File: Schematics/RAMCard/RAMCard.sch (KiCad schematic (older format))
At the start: 8 parts, among them U1 74LS32, U2 74LS04, U3 IDT71256SA12TPG, U4 IDT71256SA12TPG

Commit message: Update RAMCard to include PI and PO signals.
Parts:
- removed U1: 74LS32, Package_DIP:DIP-14_W7.62mm, symbol 74xx:74LS32
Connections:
- net labels added: ~PI, ~PO
- net labels removed: DeviceSelect5, DeviceSelect[0..7], ~MI, ~MO
- wire segments 76 -> 69
- no-connect marks 16 -> 10
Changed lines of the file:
@@
 encoding utf-8
 Sheet 1 1
-Title ""
+Title "RAM Card"
 Date ""
 Rev ""
@@
 Wire Bus Line
 	5850 1250 1900 1250
-Text GLabel 1850 2000 0    50   Input ~ 0
-DeviceSelect[0..7]
-Text GLabel 1850 1700 0    50   Input ~ 0
-~MI
-$Comp
-L 74xx:74LS32 U?
-U 2 1 5E2163C3
-P 4700 2400
-AR Path="/5D2C0C74/5E2163C3" Ref="U?"  Part="1"
-AR Path="/5D2C1188/5E2163C3" Ref="U?"  Part="2"
-AR Path="/5E2163C3" Ref="U1"  Part="2"
-F 0 "U1" H 4700 2725 50  0000 C CNN
-F 1 "74LS32" H 4700 2634 50  0000 C CNN
-F 2 "Package_DIP:DIP-14_W7.62mm" H 4700 2400 50  0001 C CNN
-F 3 "http://www.ti.com/lit/gpn/sn74LS32" H 4700 2400 50  0001 C CNN
-	2    4700 2400
-	1    0    0    -1
-$EndComp
-Text GLabel 1850 2500 0    50   Input ~ 0
-~MO
-Wire Bus Line
-	1850 2000 1900 2000
-Text Label 2050 2100 0    50   ~ 0
-DeviceSelect5
-Entry Wire Line
-	1900 2000 2000 2100
-Wire Wire Line
-	4250 2100 2000 2100
-$Comp
-L 74xx:74LS32 U?
-U 1 1 5E2163CE
-P 4700 1800
-AR Path="/5D2C0C74/5E2163CE" Ref="U?"  Part="1"
-AR Path="/5D2C1188/5E2163CE" Ref="U?"  Part="1"
-AR Path="/5E2163CE" Ref="U1"  Part="1"
-F 0 "U1" H 4700 2125 50  0000 C CNN
-F 1 "74LS32" H 4700 2034 50  0000 C CNN
-F 2 "Package_DIP:DIP-14_W7.62mm" H 4700 1800 50  0001 C CNN
-F 3 "http://www.ti.com/lit/gpn/sn74LS32" H 4700 1800 50  0001 C CNN
-	1    4700 1800
-	1    0    0    -1
-$EndComp
-Wire Wire Line
-	4400 1700 1850 1700
-Wire Wire Line
-	4400 1900 4250 1900
-Wire Wire Line
-	4250 1900 4250 2100
-Wire Wire Line
-	1850 2500 4400 2500
-Wire Wire Line
-	4250 2100 4250 2300
-Wire Wire Line
-	4250 2300 4400 2300
-Connection ~ 4250 2100
-Wire Wire Line
-	5000 1800 5700 1800
+Text GLabel 1850 1800 0    50   Input ~ 0
+~PI
+Text GLabel 1850 2400 0    50   Input ~ 0
+~PO
 Wire Wire Line
 	5700 1800 5700 2050
@@
 	5700 4350 5700 2050
 Connection ~ 5700 2050
-Wire Wire Line
-	5000 2400 5600 2400
 Wire Wire Line
 	5600 2400 5600 4450
@@
 Connection ~ 800  7750
 $Comp
-L 74xx:74LS32 U?
-U 3 1 5DB5AC2C
-P -1250 3150
-AR Path="/5D2C0C74/5DB5AC2C" Ref="U?"  Part="1"
-AR Path="/5D2C1188/5DB5AC2C" Ref="U?"  Part="3"
-AR Path="/5DB5AC2C" Ref="U1"  Part="3"
-F 0 "U1" H -1250 3475 50  0000 C CNN
-F 1 "74LS32" H -1250 3384 50  0000 C CNN
-F 2 "Package_DIP:DIP-14_W7.62mm" H -1250 3150 50  0001 C CNN
-F 3 "http://www.ti.com/lit/gpn/sn74LS32" H -1250 3150 50  0001 C CNN
-	3    -1250 3150
-	1    0    0    -1
-$EndComp
-$Comp
-L 74xx:74LS32 U?
-U 4 1 5DB5BEE6
-P -1250 3700
-AR Path="/5D2C0C74/5DB5BEE6" Ref="U?"  Part="1"
-AR Path="/5D2C1188/5DB5BEE6" Ref="U?"  Part="4"
-AR Path="/5DB5BEE6" Ref="U1"  Part="4"
-F 0 "U1" H -1250 4025 50  0000 C CNN
-F 1 "74LS32" H -1250 3934 50  0000 C CNN
-F 2 "Package_DIP:DIP-14_W7.62mm" H -1250 3700 50  0001 C CNN
-F 3 "http://www.ti.com/lit/gpn/sn74LS32" H -1250 3700 50  0001 C CNN
-	4    -1250 3700
-	1    0    0    -1
-$EndComp
-NoConn ~ -1550 3050
-NoConn ~ -1550 3250
-NoConn ~ -1550 3600
-NoConn ~ -1550 3800
-NoConn ~ -950 3700
-NoConn ~ -950 3150
-$Comp
 L 74xx:74LS04 U2
 U 4 1 5DB73163
@@
 NoConn ~ -250 4850
 NoConn ~ -250 4350
+Wire Wire Line
+	1850 2400 5600 2400
+Wire Wire Line
+	1850 1800 5700 1800
 Wire Bus Line
 	5850 1250 5850 5350

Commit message: Layout a PCB for the RAM card
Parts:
- removed C4: 100nF, Capacitor_THT:C_Disc_D4.3mm_W1.9mm_P5.00mm, symbol Device:C
- removed unit 2 of U2
- removed unit 4 of U2
- removed unit 3 of U2
- removed unit 5 of U2
- removed unit 6 of U2
- added J1: Device 2, Connector_PinHeader_2.54mm:PinHeader_2x20_P2.54mm_Horizontal, symbol Connector_Generic:Conn_02x20_Top_Bottom
- renumbered U2 to U1, U3 to U2, U4 to U3
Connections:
- net AddressBus0: now also J1.3 (Pin_3)
- net AddressBus1: now also J1.4 (Pin_4)
- net AddressBus10: now also J1.13 (Pin_13)
- net AddressBus11: now also J1.14 (Pin_14)
- net AddressBus12: now also J1.15 (Pin_15)
- net AddressBus13: now also J1.16 (Pin_16)
- net AddressBus14: now also J1.17 (Pin_17)
- net AddressBus15: now also J1.18 (Pin_18)
- net AddressBus2: now also J1.5 (Pin_5)
- net AddressBus3: now also J1.6 (Pin_6)
- net AddressBus4: now also J1.7 (Pin_7)
- net AddressBus5: now also J1.8 (Pin_8)
- net AddressBus6: now also J1.9 (Pin_9)
- net AddressBus7: now also J1.10 (Pin_10)
- net AddressBus8: now also J1.11 (Pin_11)
- net AddressBus9: now also J1.12 (Pin_12)
- net DataBus0: now also J1.21 (Pin_21)
- net DataBus1: now also J1.22 (Pin_22)
- net DataBus2: now also J1.23 (Pin_23)
- net DataBus3: now also J1.24 (Pin_24)
- net DataBus4: now also J1.25 (Pin_25)
- net DataBus5: now also J1.26 (Pin_26)
- net DataBus6: now also J1.27 (Pin_27)
- net DataBus7: now also J1.28 (Pin_28)
- net GND: now also J1.1 (Pin_1), J1.31 (Pin_31), J1.32 (Pin_32), J1.33 (Pin_33), J1.34 (Pin_34), J1.35 (Pin_35), J1.36 (Pin_36), J1.37 (Pin_37), J1.38 (Pin_38), J1.39 (Pin_39), J1.40 (Pin_40)
- net VCC: now also J1.2 (Pin_2); no longer C1.1, C2.1, C3.1
- net ~PI: now also J1.29 (Pin_29)
- net ~PO: now also J1.30 (Pin_30)
- new net: C1.1, C2.1, C3.1
- no-connect marks 10 -> 2
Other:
- moved on the sheet: U1A, U2, U3

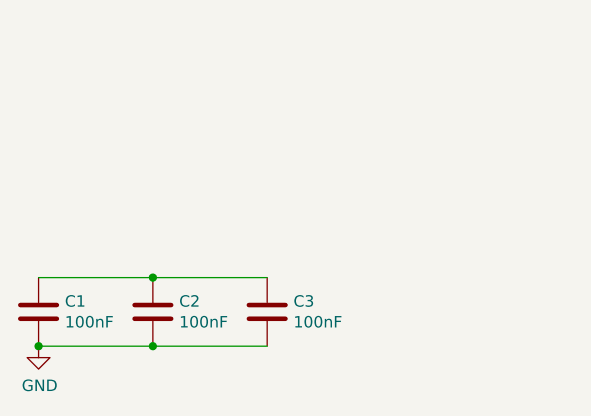
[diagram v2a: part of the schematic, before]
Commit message: Fix RAM card DRC errors
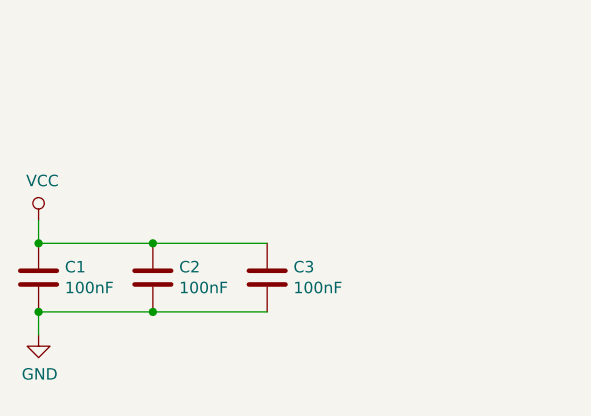
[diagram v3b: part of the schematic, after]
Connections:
- net VCC: now also C1.1, C2.1, C3.1
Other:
- moved on the sheet: C1, C2, C3
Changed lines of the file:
@@
 L Device:C C?
 U 1 1 5E262247
-P 800 7600
+P 800 7450
 AR Path="/5D2C07CD/5E262247" Ref="C?"  Part="1"
 AR Path="/5D2C1188/5E262247" Ref="C?"  Part="1"
 AR Path="/5E262247" Ref="C1"  Part="1"
-F 0 "C1" H 915 7646 50  0000 L CNN
-F 1 "100nF" H 915 7555 50  0000 L CNN
-F 2 "Capacitor_THT:C_Disc_D4.3mm_W1.9mm_P5.00mm" H 838 7450 50  0001 C CNN
-F 3 "~" H 800 7600 50  0001 C CNN
-	1    800  7600
+F 0 "C1" H 915 7496 50  0000 L CNN
+F 1 "100nF" H 915 7405 50  0000 L CNN
+F 2 "Capacitor_THT:C_Disc_D4.3mm_W1.9mm_P5.00mm" H 838 7300 50  0001 C CNN
+F 3 "~" H 800 7450 50  0001 C CNN
+	1    800  7450
 	1    0    0    -1
 $EndComp
@@
 L Device:C C?
 U 1 1 5E26224D
-P 1300 7600
+P 1300 7450
 AR Path="/5D2C07CD/5E26224D" Ref="C?"  Part="1"
 AR Path="/5D2C1188/5E26224D" Ref="C?"  Part="1"
 AR Path="/5E26224D" Ref="C2"  Part="1"
-F 0 "C2" H 1415 7646 50  0000 L CNN
-F 1 "100nF" H 1415 7555 50  0000 L CNN
-F 2 "Capacitor_THT:C_Disc_D4.3mm_W1.9mm_P5.00mm" H 1338 7450 50  0001 C CNN
-F 3 "~" H 1300 7600 50  0001 C CNN
-	1    1300 7600
+F 0 "C2" H 1415 7496 50  0000 L CNN
+F 1 "100nF" H 1415 7405 50  0000 L CNN
+F 2 "Capacitor_THT:C_Disc_D4.3mm_W1.9mm_P5.00mm" H 1338 7300 50  0001 C CNN
+F 3 "~" H 1300 7450 50  0001 C CNN
+	1    1300 7450
 	1    0    0    -1
 $EndComp
@@
 L Device:C C?
 U 1 1 5E262253
-P 1800 7600
+P 1800 7450
 AR Path="/5D2C07CD/5E262253" Ref="C?"  Part="1"
 AR Path="/5D2C1188/5E262253" Ref="C?"  Part="1"
 AR Path="/5E262253" Ref="C3"  Part="1"
-F 0 "C3" H 1915 7646 50  0000 L CNN
-F 1 "100nF" H 1915 7555 50  0000 L CNN
-F 2 "Capacitor_THT:C_Disc_D4.3mm_W1.9mm_P5.00mm" H 1838 7450 50  0001 C CNN
-F 3 "~" H 1800 7600 50  0001 C CNN
-	1    1800 7600
+F 0 "C3" H 1915 7496 50  0000 L CNN
+F 1 "100nF" H 1915 7405 50  0000 L CNN
+F 2 "Capacitor_THT:C_Disc_D4.3mm_W1.9mm_P5.00mm" H 1838 7300 50  0001 C CNN
+F 3 "~" H 1800 7450 50  0001 C CNN
+	1    1800 7450
 	1    0    0    -1
 $EndComp
@@
 L power:GND #PWR?
 U 1 1 5E26225F
-P 800 7750
+P 800 7700
 AR Path="/5D2C07CD/5E26225F" Ref="#PWR?"  Part="1"
 AR Path="/5D2C1188/5E26225F" Ref="#PWR?"  Part="1"
 AR Path="/5E26225F" Ref="#PWR01"  Part="1"
-F 0 "#PWR01" H 800 7500 50  0001 C CNN
-F 1 "GND" H 805 7577 50  0000 C CNN
-F 2 "" H 800 7750 50  0001 C CNN
-F 3 "" H 800 7750 50  0001 C CNN
-	1    800  7750
-	1    0    0    -1
-$EndComp
-Wire Wire Line
-	800  7450 1300 7450
-Wire Wire Line
-	1300 7450 1800 7450
-Connection ~ 1300 7450
-Wire Wire Line
-	1800 7750 1300 7750
-Wire Wire Line
-	1300 7750 800  7750
-Connection ~ 1300 7750
-Connection ~ 800  7750
+F 0 "#PWR01" H 800 7450 50  0001 C CNN
+F 1 "GND" H 805 7527 50  0000 C CNN
+F 2 "" H 800 7700 50  0001 C CNN
+F 3 "" H 800 7700 50  0001 C CNN
+	1    800  7700
+	1    0    0    -1
+$EndComp
+Wire Wire Line
+	800  7300 1300 7300
+Wire Wire Line
+	1300 7300 1800 7300
+Connection ~ 1300 7300
+Wire Wire Line
+	1800 7600 1300 7600
+Wire Wire Line
+	1300 7600 800  7600
+Connection ~ 1300 7600
 Entry Wire Line
 	2250 4250 2350 4150
@@
 Wire Bus Line
 	6700 1200 4050 1200
+$Comp
+L power:VCC #PWR?
+U 1 1 5D9DE32A
+P 800 7200
+F 0 "#PWR?" H 800 7050 50  0001 C CNN
+F 1 "VCC" H 817 7373 50  0000 C CNN
+F 2 "" H 800 7200 50  0001 C CNN
+F 3 "" H 800 7200 50  0001 C CNN
+	1    800  7200
+	1    0    0    -1
+$EndComp
+Wire Wire Line
+	800  7200 800  7300
+Connection ~ 800  7300
+Wire Wire Line
+	800  7600 800  7700
+Connection ~ 800  7600
 Wire Bus Line
 	4050 1200 4050 3050

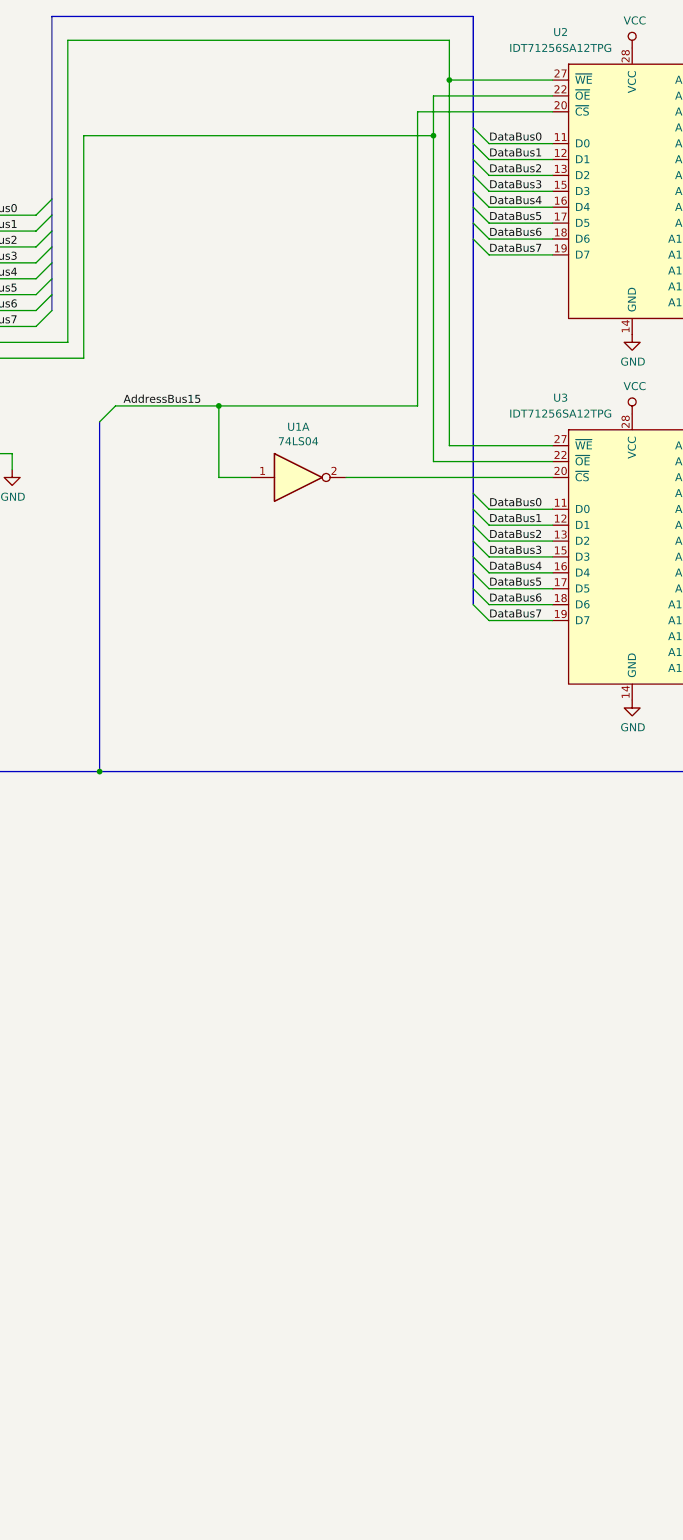
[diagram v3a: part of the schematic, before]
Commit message: RAMCard: unused inputs are tied to VCC, unused outputs are left disconnected.
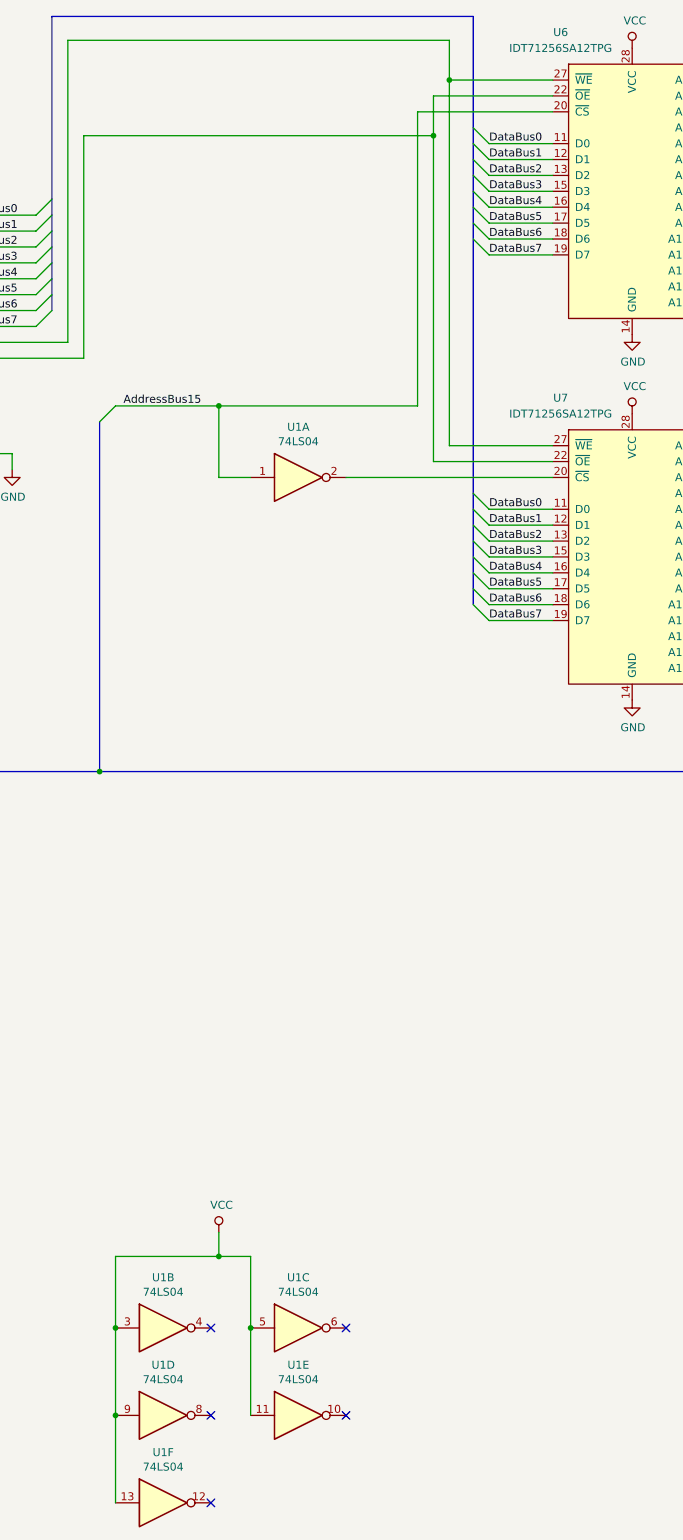
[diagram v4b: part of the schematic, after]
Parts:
- added unit 2 of U1
- added unit 3 of U1
- added unit 4 of U1
- added unit 5 of U1
- added unit 6 of U1
- renumbered U2 to U6, U3 to U7
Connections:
- net VCC: now also U1.11, U1.13, U1.3, U1.5, U1.9
- no-connect marks 2 -> 7
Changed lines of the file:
@@
 $EndDescr
 $Comp
-L Memory_RAM:IDT71256SA12TPG U2
+L Memory_RAM:IDT71256SA12TPG U6
 U 1 1 5E1E9FA0
 P 7700 2250
-F 0 "U2" H 7250 3200 50  0000 C CNN
+F 0 "U6" H 7250 3200 50  0000 C CNN
 F 1 "IDT71256SA12TPG" H 7250 3100 50  0000 C CNN
 F 2 "Package_DIP:DIP-28_W7.62mm_Socket" H 7700 4250 50  0001 C CNN
@@
 $EndComp
 $Comp
-L Memory_RAM:IDT71256SA12TPG U3
+L Memory_RAM:IDT71256SA12TPG U7
 U 1 1 5E1EC273
 P 7700 4550
-F 0 "U3" H 7250 5500 50  0000 C CNN
+F 0 "U7" H 7250 5500 50  0000 C CNN
 F 1 "IDT71256SA12TPG" H 7250 5400 50  0000 C CNN
 F 2 "Package_DIP:DIP-28_W7.62mm_Socket" H 7700 6550 50  0001 C CNN
@@
 $EndComp
 $Comp
-L power:GND #PWR06
+L power:GND #PWR08
 U 1 1 5E1EE0BF
 P 7700 3200
-F 0 "#PWR06" H 7700 2950 50  0001 C CNN
+F 0 "#PWR08" H 7700 2950 50  0001 C CNN
 F 1 "GND" H 7705 3027 50  0000 C CNN
 F 2 "" H 7700 3200 50  0001 C CNN
@@
 $EndComp
 $Comp
-L power:GND #PWR08
+L power:GND #PWR010
 U 1 1 5E1EE650
 P 7700 5500
-F 0 "#PWR08" H 7700 5250 50  0001 C CNN
+F 0 "#PWR010" H 7700 5250 50  0001 C CNN
 F 1 "GND" H 7705 5327 50  0000 C CNN
 F 2 "" H 7700 5500 50  0001 C CNN
@@
 $EndComp
 $Comp
-L power:VCC #PWR07
+L power:VCC #PWR09
 U 1 1 5E1EEC64
 P 7700 3700
-F 0 "#PWR07" H 7700 3550 50  0001 C CNN
+F 0 "#PWR09" H 7700 3550 50  0001 C CNN
 F 1 "VCC" H 7717 3873 50  0000 C CNN
 F 2 "" H 7700 3700 50  0001 C CNN
@@
 $EndComp
 $Comp
-L power:VCC #PWR05
+L power:VCC #PWR07
 U 1 1 5E1EF332
 P 7700 1400
-F 0 "#PWR05" H 7700 1250 50  0001 C CNN
+F 0 "#PWR07" H 7700 1250 50  0001 C CNN
 F 1 "VCC" H 7717 1573 50  0000 C CNN
 F 2 "" H 7700 1400 50  0001 C CNN
@@
 AR Path="/5D2C07CD/5E26225F" Ref="#PWR?"  Part="1"
 AR Path="/5D2C1188/5E26225F" Ref="#PWR?"  Part="1"
-AR Path="/5E26225F" Ref="#PWR01"  Part="1"
-F 0 "#PWR01" H 800 7450 50  0001 C CNN
+AR Path="/5E26225F" Ref="#PWR02"  Part="1"
+F 0 "#PWR02" H 800 7450 50  0001 C CNN
 F 1 "GND" H 805 7527 50  0000 C CNN
 F 2 "" H 800 7700 50  0001 C CNN
@@
 	3550 3750 3550 3850
 $Comp
-L power:GND #PWR04
+L power:GND #PWR05
 U 1 1 5E55ACB0
 P 3800 4050
-F 0 "#PWR04" H 3800 3800 50  0001 C CNN
+F 0 "#PWR05" H 3800 3800 50  0001 C CNN
 F 1 "GND" H 3805 3877 50  0000 C CNN
 F 2 "" H 3800 4050 50  0001 C CNN
@@
 	3800 3950 3800 4050
 $Comp
-L power:GND #PWR03
+L power:GND #PWR04
 U 1 1 5EB03C95
 P 2850 2450
-F 0 "#PWR03" H 2850 2200 50  0001 C CNN
+F 0 "#PWR04" H 2850 2200 50  0001 C CNN
 F 1 "GND" H 2855 2277 50  0000 C CNN
 F 2 "" H 2850 2450 50  0001 C CNN
@@
 	2850 2450 2950 2450
 $Comp
-L power:VCC #PWR02
+L power:VCC #PWR03
 U 1 1 5EB25931
 P 2600 2450
-F 0 "#PWR02" H 2600 2300 50  0001 C CNN
+F 0 "#PWR03" H 2600 2300 50  0001 C CNN
 F 1 "VCC" H 2617 2623 50  0000 C CNN
 F 2 "" H 2600 2450 50  0001 C CNN
@@
 	6700 1200 4050 1200
 $Comp
-L power:VCC #PWR?
+L power:VCC #PWR01
 U 1 1 5D9DE32A
 P 800 7200
-F 0 "#PWR?" H 800 7050 50  0001 C CNN
+F 0 "#PWR01" H 800 7050 50  0001 C CNN
 F 1 "VCC" H 817 7373 50  0000 C CNN
 F 2 "" H 800 7200 50  0001 C CNN
@@
 	800  7600 800  7700
 Connection ~ 800  7600
+$Comp
+L 74xx:74LS04 U1
+U 2 1 5D9F1673
+P 4750 9450
+F 0 "U1" H 4750 9767 50  0000 C CNN
+F 1 "74LS04" H 4750 9676 50  0000 C CNN
+F 2 "Package_DIP:DIP-14_W7.62mm" H 4750 9450 50  0001 C CNN
+F 3 "http://www.ti.com/lit/gpn/sn74LS04" H 4750 9450 50  0001 C CNN
+	2    4750 9450
+	1    0    0    -1
+$EndComp
+$Comp
+L 74xx:74LS04 U1
+U 3 1 5D9F27D4
+P 5600 9450
+F 0 "U1" H 5600 9767 50  0000 C CNN
+F 1 "74LS04" H 5600 9676 50  0000 C CNN
+F 2 "Package_DIP:DIP-14_W7.62mm" H 5600 9450 50  0001 C CNN
+F 3 "http://www.ti.com/lit/gpn/sn74LS04" H 5600 9450 50  0001 C CNN
+	3    5600 9450
+	1    0    0    -1
+$EndComp
+$Comp
+L 74xx:74LS04 U1
+U 5 1 5D9F469A
+P 5600 10000
+F 0 "U1" H 5600 10317 50  0000 C CNN
+F 1 "74LS04" H 5600 10226 50  0000 C CNN
+F 2 "Package_DIP:DIP-14_W7.62mm" H 5600 10000 50  0001 C CNN
+F 3 "http://www.ti.com/lit/gpn/sn74LS04" H 5600 10000 50  0001 C CNN
+	5    5600 10000
+	1    0    0    -1
+$EndComp
+NoConn ~ 5050 9450
+NoConn ~ 5900 9450
+NoConn ~ 5900 10000
+NoConn ~ 5050 10000
+$Comp
+L power:VCC #PWR06
+U 1 1 5DA12FF5
+P 5100 8850
+F 0 "#PWR06" H 5100 8700 50  0001 C CNN
+F 1 "VCC" H 5117 9023 50  0000 C CNN
+F 2 "" H 5100 8850 50  0001 C CNN
+F 3 "" H 5100 8850 50  0001 C CNN
+	1    5100 8850
+	1    0    0    -1
+$EndComp
+Wire Wire Line
+	4450 10000 4450 9450
+Wire Wire Line
+	4450 9000 5100 9000
+Wire Wire Line
+	5100 9000 5100 8850
+Connection ~ 4450 9450
+Wire Wire Line
+	4450 9450 4450 9000
+Wire Wire Line
+	5100 9000 5300 9000
+Wire Wire Line
+	5300 9000 5300 9450
+Connection ~ 5100 9000
+Connection ~ 5300 9450
+Wire Wire Line
+	5300 9450 5300 10000
+$Comp
+L 74xx:74LS04 U1
+U 6 1 5DA23B9A
+P 4750 10550
+F 0 "U1" H 4750 10867 50  0000 C CNN
+F 1 "74LS04" H 4750 10776 50  0000 C CNN
+F 2 "Package_DIP:DIP-14_W7.62mm" H 4750 10550 50  0001 C CNN
+F 3 "http://www.ti.com/lit/gpn/sn74LS04" H 4750 10550 50  0001 C CNN
+	6    4750 10550
+	1    0    0    -1
+$EndComp
+Wire Wire Line
+	4450 10550 4450 10000
+Connection ~ 4450 10000
+$Comp
+L 74xx:74LS04 U1
+U 4 1 5D9F3A1C
+P 4750 10000
+F 0 "U1" H 4750 10317 50  0000 C CNN
+F 1 "74LS04" H 4750 10226 50  0000 C CNN
+F 2 "Package_DIP:DIP-14_W7.62mm" H 4750 10000 50  0001 C CNN
+F 3 "http://www.ti.com/lit/gpn/sn74LS04" H 4750 10000 50  0001 C CNN
+	4    4750 10000
+	1    0    0    -1
+$EndComp
+NoConn ~ 5050 10550
 Wire Bus Line
 	4050 1200 4050 3050
